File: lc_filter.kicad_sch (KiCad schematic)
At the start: 8 parts

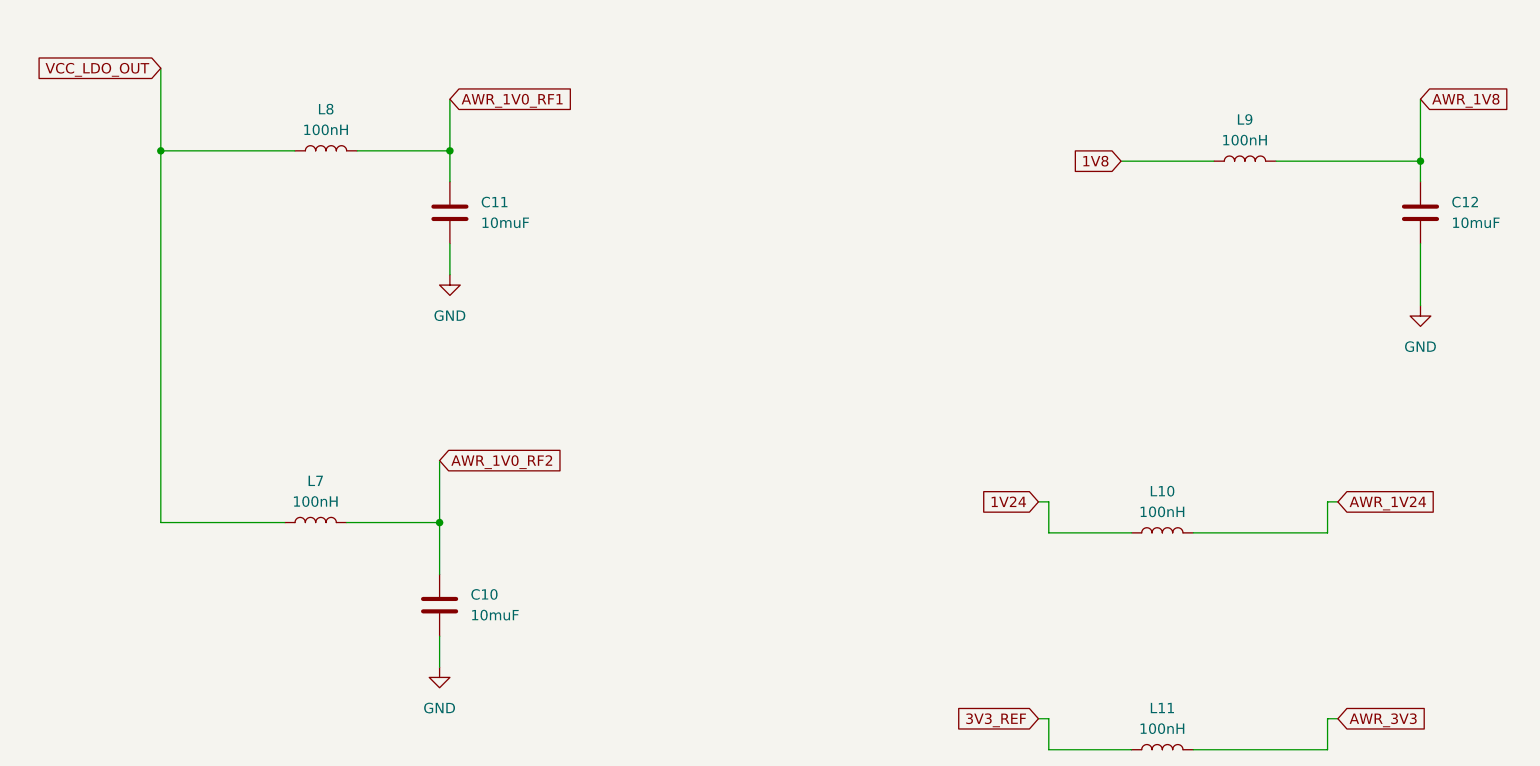
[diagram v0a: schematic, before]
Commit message: squashed ERC errors, moving onto pcb, grabbing fuse footprint
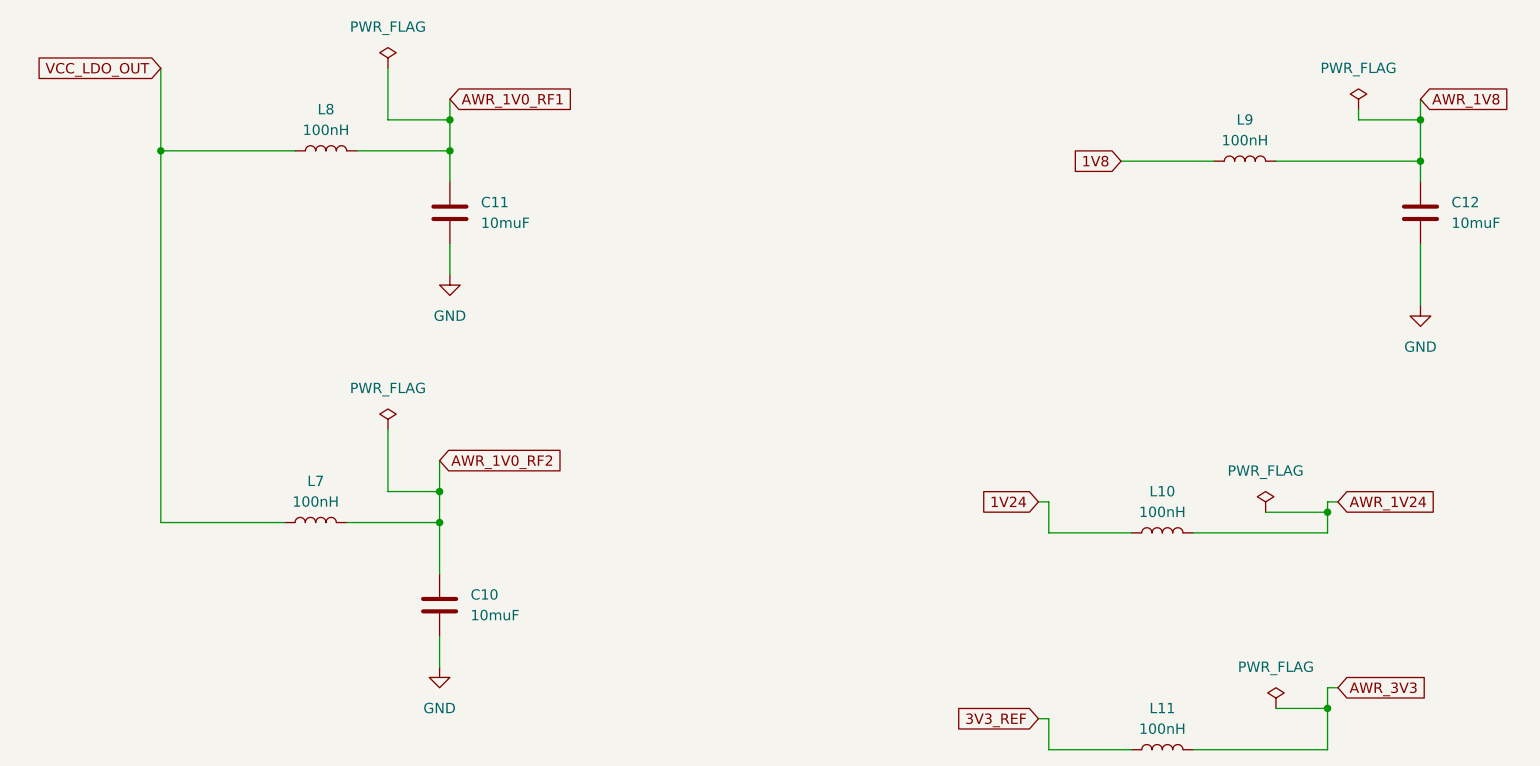
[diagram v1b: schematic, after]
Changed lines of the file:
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@@
 (kicad_sch (version 20230121) (generator eeschema)
   (paper "A4")
+  (junction (at 82.55 35.56) (diameter 0) (color 0 0 0 0)
+  )
   (junction (at 82.55 39.37) (diameter 0) (color 0 0 0 0)
   )
+  (junction (at 201.93 35.56) (diameter 0) (color 0 0 0 0)
+  )
   (junction (at 201.93 40.64) (diameter 0) (color 0 0 0 0)
   )
+  (junction (at 81.28 81.28) (diameter 0) (color 0 0 0 0)
+  )
+  (junction (at 190.5 83.82) (diameter 0) (color 0 0 0 0)
+  )
   (junction (at 81.28 85.09) (diameter 0) (color 0 0 0 0)
   )
+  (junction (at 190.5 107.95) (diameter 0) (color 0 0 0 0)
+  )
   (junction (at 46.99 39.37) (diameter 0) (color 0 0 0 0)
   )
-  (wire (pts (xy 190.5 82.55) (xy 190.5 86.36))
-    (stroke (width 0) (type default))
-  )
-  (wire (pts (xy 190.5 86.36) (xy 173.99 86.36))
-    (stroke (width 0) (type default))
-  )
-  (wire (pts (xy 201.93 40.64) (xy 201.93 33.02))
+  (wire (pts (xy 190.5 82.55) (xy 190.5 83.82))
+    (stroke (width 0) (type default))
+  )
+  (wire (pts (xy 190.5 107.95) (xy 190.5 113.03))
+    (stroke (width 0) (type default))
+  )
+  (wire (pts (xy 173.99 86.36) (xy 190.5 86.36))
+    (stroke (width 0) (type default))
+  )
+  (wire (pts (xy 201.93 40.64) (xy 201.93 35.56))
+    (stroke (width 0) (type default))
+  )
+  (wire (pts (xy 190.5 83.82) (xy 190.5 86.36))
     (stroke (width 0) (type default))
   )
@@
     (stroke (width 0) (type default))
   )
-  (wire (pts (xy 81.28 77.47) (xy 81.28 85.09))
+  (wire (pts (xy 74.93 35.56) (xy 74.93 29.21))
     (stroke (width 0) (type default))
   )
@@
     (stroke (width 0) (type default))
   )
+  (wire (pts (xy 81.28 77.47) (xy 81.28 81.28))
+    (stroke (width 0) (type default))
+  )
   (wire (pts (xy 184.15 40.64) (xy 201.93 40.64))
     (stroke (width 0) (type default))
   )
-  (wire (pts (xy 190.5 109.22) (xy 191.77 109.22))
+  (wire (pts (xy 190.5 105.41) (xy 191.77 105.41))
     (stroke (width 0) (type default))
   )
@@
     (stroke (width 0) (type default))
   )
+  (wire (pts (xy 82.55 35.56) (xy 82.55 39.37))
+    (stroke (width 0) (type default))
+  )
   (wire (pts (xy 69.85 85.09) (xy 81.28 85.09))
     (stroke (width 0) (type default))
   )
+  (wire (pts (xy 184.15 107.95) (xy 190.5 107.95))
+    (stroke (width 0) (type default))
+  )
+  (wire (pts (xy 182.88 83.82) (xy 190.5 83.82))
+    (stroke (width 0) (type default))
+  )
   (wire (pts (xy 46.99 39.37) (xy 46.99 85.09))
     (stroke (width 0) (type default))
@@
     (stroke (width 0) (type default))
   )
-  (wire (pts (xy 190.5 113.03) (xy 173.99 113.03))
-    (stroke (width 0) (type default))
-  )
-  (wire (pts (xy 82.55 33.02) (xy 82.55 39.37))
+  (wire (pts (xy 173.99 113.03) (xy 190.5 113.03))
+    (stroke (width 0) (type default))
+  )
+  (wire (pts (xy 82.55 33.02) (xy 82.55 35.56))
+    (stroke (width 0) (type default))
+  )
+  (wire (pts (xy 81.28 81.28) (xy 81.28 85.09))
     (stroke (width 0) (type default))
   )
@@
     (stroke (width 0) (type default))
   )
+  (wire (pts (xy 82.55 35.56) (xy 74.93 35.56))
+    (stroke (width 0) (type default))
+  )
   (wire (pts (xy 190.5 82.55) (xy 191.77 82.55))
     (stroke (width 0) (type default))
@@
     (stroke (width 0) (type default))
   )
-  (wire (pts (xy 190.5 109.22) (xy 190.5 113.03))
+  (wire (pts (xy 81.28 81.28) (xy 74.93 81.28))
+    (stroke (width 0) (type default))
+  )
+  (wire (pts (xy 201.93 35.56) (xy 194.31 35.56))
+    (stroke (width 0) (type default))
+  )
+  (wire (pts (xy 74.93 81.28) (xy 74.93 73.66))
+    (stroke (width 0) (type default))
+  )
+  (wire (pts (xy 194.31 35.56) (xy 194.31 34.29))
+    (stroke (width 0) (type default))
+  )
+  (wire (pts (xy 190.5 105.41) (xy 190.5 107.95))
     (stroke (width 0) (type default))
   )
@@
     (stroke (width 0) (type default))
   )
+  (wire (pts (xy 71.12 39.37) (xy 82.55 39.37))
+    (stroke (width 0) (type default))
+  )
   (wire (pts (xy 156.21 113.03) (xy 166.37 113.03))
     (stroke (width 0) (type default))
@@
     (stroke (width 0) (type default))
   )
-  (wire (pts (xy 82.55 39.37) (xy 71.12 39.37))
-    (stroke (width 0) (type default))
-  )
   (wire (pts (xy 201.93 50.8) (xy 201.93 58.42))
+    (stroke (width 0) (type default))
+  )
+  (wire (pts (xy 201.93 35.56) (xy 201.93 33.02))
     (stroke (width 0) (type default))
   )
@@
     )
   )
-  (global_label "AWR_3V3" (shape input) (at 191.77 109.22 0) (fields_autoplaced)
+  (global_label "AWR_3V3" (shape input) (at 191.77 105.41 0) (fields_autoplaced)
     (effects (font (size 1.27 1.27)) (justify left))
-    (property "Intersheetrefs" "${INTERSHEET_REFS}" (at 203.0404 109.22 0)
+    (property "Intersheetrefs" "${INTERSHEET_REFS}" (at 203.0404 105.41 0)
       (effects (font (size 1.27 1.27)) (justify left) hide)
     )
@@
     )
   )
+  (symbol (lib_id "power:PWR_FLAG") (at 74.93 29.21 0) (unit 1)
+    (in_bom yes) (on_board yes) (dnp no) (fields_autoplaced)
+    (property "Reference" "#FLG01" (at 74.93 27.305 0)
+      (effects (font (size 1.27 1.27)) hide)
+    )
+    (property "Value" "PWR_FLAG" (at 74.93 24.13 0)
+      (effects (font (size 1.27 1.27)))
+    )
+    (property "Footprint" "" (at 74.93 29.21 0)
+      (effects (font (size 1.27 1.27)) hide)
+    )
+    (property "Datasheet" "~" (at 74.93 29.21 0)
+      (effects (font (size 1.27 1.27)) hide)
+    )
+    (pin "1")
+    (instances
+      (project "radar"
+        (path "/88b309aa-5f0e-45d7-beec-81d4b0ee2121/7a3c78f1-80f2-463b-a37f-9a7b3cc7f964/49f03812-e634-4c1d-a083-41410e96c5c9"
+          (reference "#FLG01") (unit 1)
+        )
+      )
+    )
+  )
+  (symbol (lib_id "power:PWR_FLAG") (at 74.93 73.66 0) (unit 1)
+    (in_bom yes) (on_board yes) (dnp no) (fields_autoplaced)
+    (property "Reference" "#FLG02" (at 74.93 71.755 0)
+      (effects (font (size 1.27 1.27)) hide)
+    )
+    (property "Value" "PWR_FLAG" (at 74.93 68.58 0)
+      (effects (font (size 1.27 1.27)))
+    )
+    (property "Footprint" "" (at 74.93 73.66 0)
+      (effects (font (size 1.27 1.27)) hide)
+    )
+    (property "Datasheet" "~" (at 74.93 73.66 0)
+      (effects (font (size 1.27 1.27)) hide)
+    )
+    (pin "1")
+    (instances
+      (project "radar"
+        (path "/88b309aa-5f0e-45d7-beec-81d4b0ee2121/7a3c78f1-80f2-463b-a37f-9a7b3cc7f964/49f03812-e634-4c1d-a083-41410e96c5c9"
+          (reference "#FLG02") (unit 1)
+        )
+      )
+    )
+  )
+  (symbol (lib_id "power:PWR_FLAG") (at 194.31 34.29 0) (unit 1)
+    (in_bom yes) (on_board yes) (dnp no) (fields_autoplaced)
+    (property "Reference" "#FLG04" (at 194.31 32.385 0)
+      (effects (font (size 1.27 1.27)) hide)
+    )
+    (property "Value" "PWR_FLAG" (at 194.31 29.21 0)
+      (effects (font (size 1.27 1.27)))
+    )
+    (property "Footprint" "" (at 194.31 34.29 0)
+      (effects (font (size 1.27 1.27)) hide)
+    )
+    (property "Datasheet" "~" (at 194.31 34.29 0)
+      (effects (font (size 1.27 1.27)) hide)
+    )
+    (pin "1")
+    (instances
+      (project "radar"
+        (path "/88b309aa-5f0e-45d7-beec-81d4b0ee2121/7a3c78f1-80f2-463b-a37f-9a7b3cc7f964/49f03812-e634-4c1d-a083-41410e96c5c9"
+          (reference "#FLG04") (unit 1)
+        )
+      )
+    )
+  )
   (symbol (lib_id "Device:C") (at 81.28 95.25 0) (unit 1)
     (in_bom yes) (on_board yes) (dnp no) (fields_autoplaced)
@@
     )
   )
+  (symbol (lib_id "power:PWR_FLAG") (at 182.88 83.82 0) (unit 1)
+    (in_bom yes) (on_board yes) (dnp no) (fields_autoplaced)
+    (property "Reference" "#FLG03" (at 182.88 81.915 0)
+      (effects (font (size 1.27 1.27)) hide)
+    )
+    (property "Value" "PWR_FLAG" (at 182.88 78.74 0)
+      (effects (font (size 1.27 1.27)))
+    )
+    (property "Footprint" "" (at 182.88 83.82 0)
+      (effects (font (size 1.27 1.27)) hide)
+    )
+    (property "Datasheet" "~" (at 182.88 83.82 0)
+      (effects (font (size 1.27 1.27)) hide)
+    )
+    (pin "1")
+    (instances
+      (project "radar"
+        (path "/88b309aa-5f0e-45d7-beec-81d4b0ee2121/7a3c78f1-80f2-463b-a37f-9a7b3cc7f964/49f03812-e634-4c1d-a083-41410e96c5c9"
+          (reference "#FLG03") (unit 1)
+        )
+      )
+    )
+  )
   (symbol (lib_id "power:GND") (at 81.28 102.87 0) (unit 1)
     (in_bom yes) (on_board yes) (dnp no) (fields_autoplaced)
@@
         )
       )
+    )
+  )
+  (symbol (lib_id "power:PWR_FLAG") (at 184.15 107.95 0) (unit 1)
+    (in_bom yes) (on_board yes) (dnp no) (fields_autoplaced)
+    (property "Reference" "#FLG05" (at 184.15 106.045 0)
+      (effects (font (size 1.27 1.27)) hide)
+    )
+    (property "Value" "PWR_FLAG" (at 184.15 102.87 0)
+      (effects (font (size 1.27 1.27)))
+    )
+    (property "Footprint" "" (at 184.15 107.95 0)
+      (effects (font (size 1.27 1.27)) hide)
+    )
+    (property "Datasheet" "~" (at 184.15 107.95 0)
+      (effects (font (size 1.27 1.27)) hide)
+    )
+    (pin "1")
+    (instances
+      (project "radar"
+        (path "/88b309aa-5f0e-45d7-beec-81d4b0ee2121/7a3c78f1-80f2-463b-a37f-9a7b3cc7f964/49f03812-e634-4c1d-a083-41410e96c5c9"
+          (reference "#FLG05") (unit 1)
+        )
+      )

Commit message: adding footprints
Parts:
- C10, C11, C12: footprint (none) -> Capacitor_SMD:C_0603_1608Metric
- L10, L11, L7, L8, L9: footprint (none) -> Inductor_SMD:L_0603_1608Metric
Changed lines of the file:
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@@
       (effects (font (size 1.27 1.27)) (justify left))
     )
-    (property "Footprint" "" (at 82.2452 99.06 0)
+    (property "Footprint" "Capacitor_SMD:C_0603_1608Metric" (at 82.2452 99.06 0)
       (effects (font (size 1.27 1.27)) hide)
     )
@@
       (effects (font (size 1.27 1.27)))
     )
-    (property "Footprint" "" (at 170.18 86.36 0)
+    (property "Footprint" "Inductor_SMD:L_0603_1608Metric" (at 170.18 86.36 0)
       (effects (font (size 1.27 1.27)) hide)
     )
@@
       (effects (font (size 1.27 1.27)))
     )
-    (property "Footprint" "" (at 67.31 39.37 0)
+    (property "Footprint" "Inductor_SMD:L_0603_1608Metric" (at 67.31 39.37 0)
       (effects (font (size 1.27 1.27)) hide)
     )
@@
       (effects (font (size 1.27 1.27)))
     )
-    (property "Footprint" "" (at 66.04 85.09 0)
+    (property "Footprint" "Inductor_SMD:L_0603_1608Metric" (at 66.04 85.09 0)
       (effects (font (size 1.27 1.27)) hide)
     )
@@
       (effects (font (size 1.27 1.27)) (justify left))
     )
-    (property "Footprint" "" (at 202.8952 50.8 0)
+    (property "Footprint" "Capacitor_SMD:C_0603_1608Metric" (at 202.8952 50.8 0)
       (effects (font (size 1.27 1.27)) hide)
     )
@@
       (effects (font (size 1.27 1.27)))
     )
-    (property "Footprint" "" (at 170.18 113.03 0)
+    (property "Footprint" "Inductor_SMD:L_0603_1608Metric" (at 170.18 113.03 0)
       (effects (font (size 1.27 1.27)) hide)
     )
@@
       (effects (font (size 1.27 1.27)))
     )
-    (property "Footprint" "" (at 180.34 40.64 0)
+    (property "Footprint" "Inductor_SMD:L_0603_1608Metric" (at 180.34 40.64 0)
       (effects (font (size 1.27 1.27)) hide)
     )
@@
       (effects (font (size 1.27 1.27)) (justify left))
     )
-    (property "Footprint" "" (at 83.5152 50.8 0)
-      (effects (font (size 1.27 1.27)) hide)
-    )
+    (property "Footprint" "Capacitor_SMD:C_0603_1608Metric" (at 83.5152 50.8 0)
+      (effects (font (size 1.27 1.27)) hide)
+    )
